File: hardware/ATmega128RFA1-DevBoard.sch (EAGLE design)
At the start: 50 parts, among them J1 ISP, J2 ARDUINO_UNO_R3, J3 POWER_JACKPTH_LOCK, U1 ATMEGA128RFA1, U2 LM1117, Y1 16MHz, Y2 32.768kHz

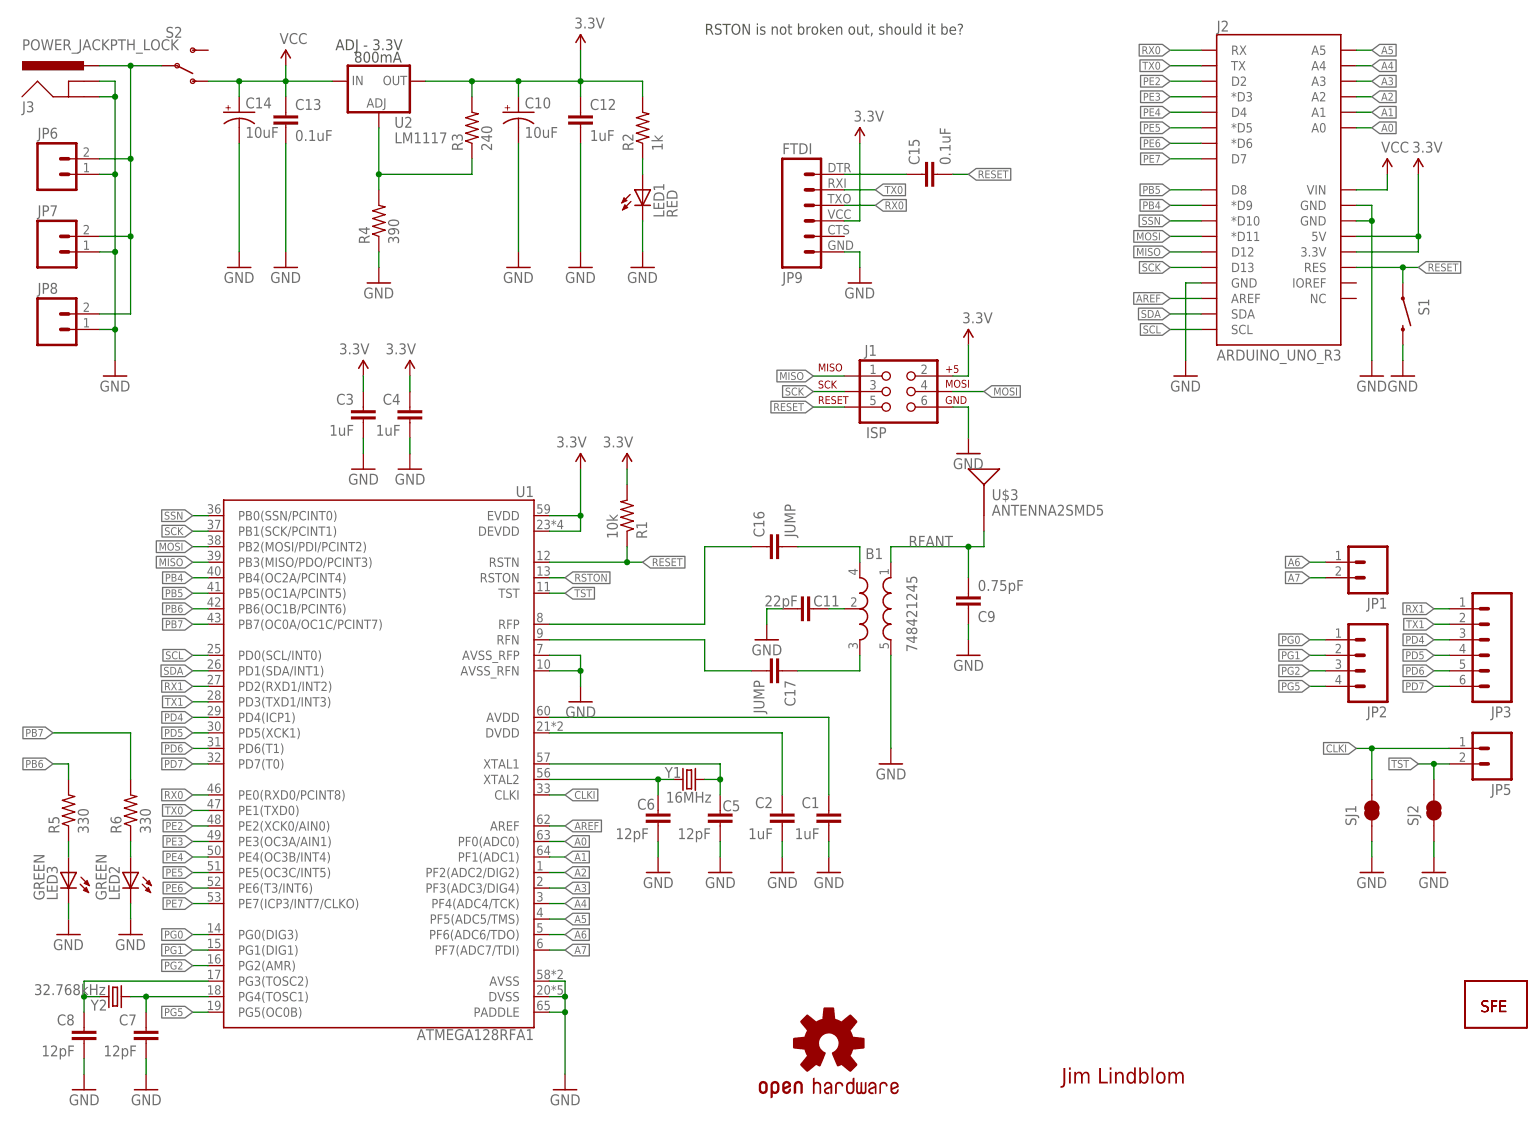
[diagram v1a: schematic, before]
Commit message: More minor silkscreen fixes
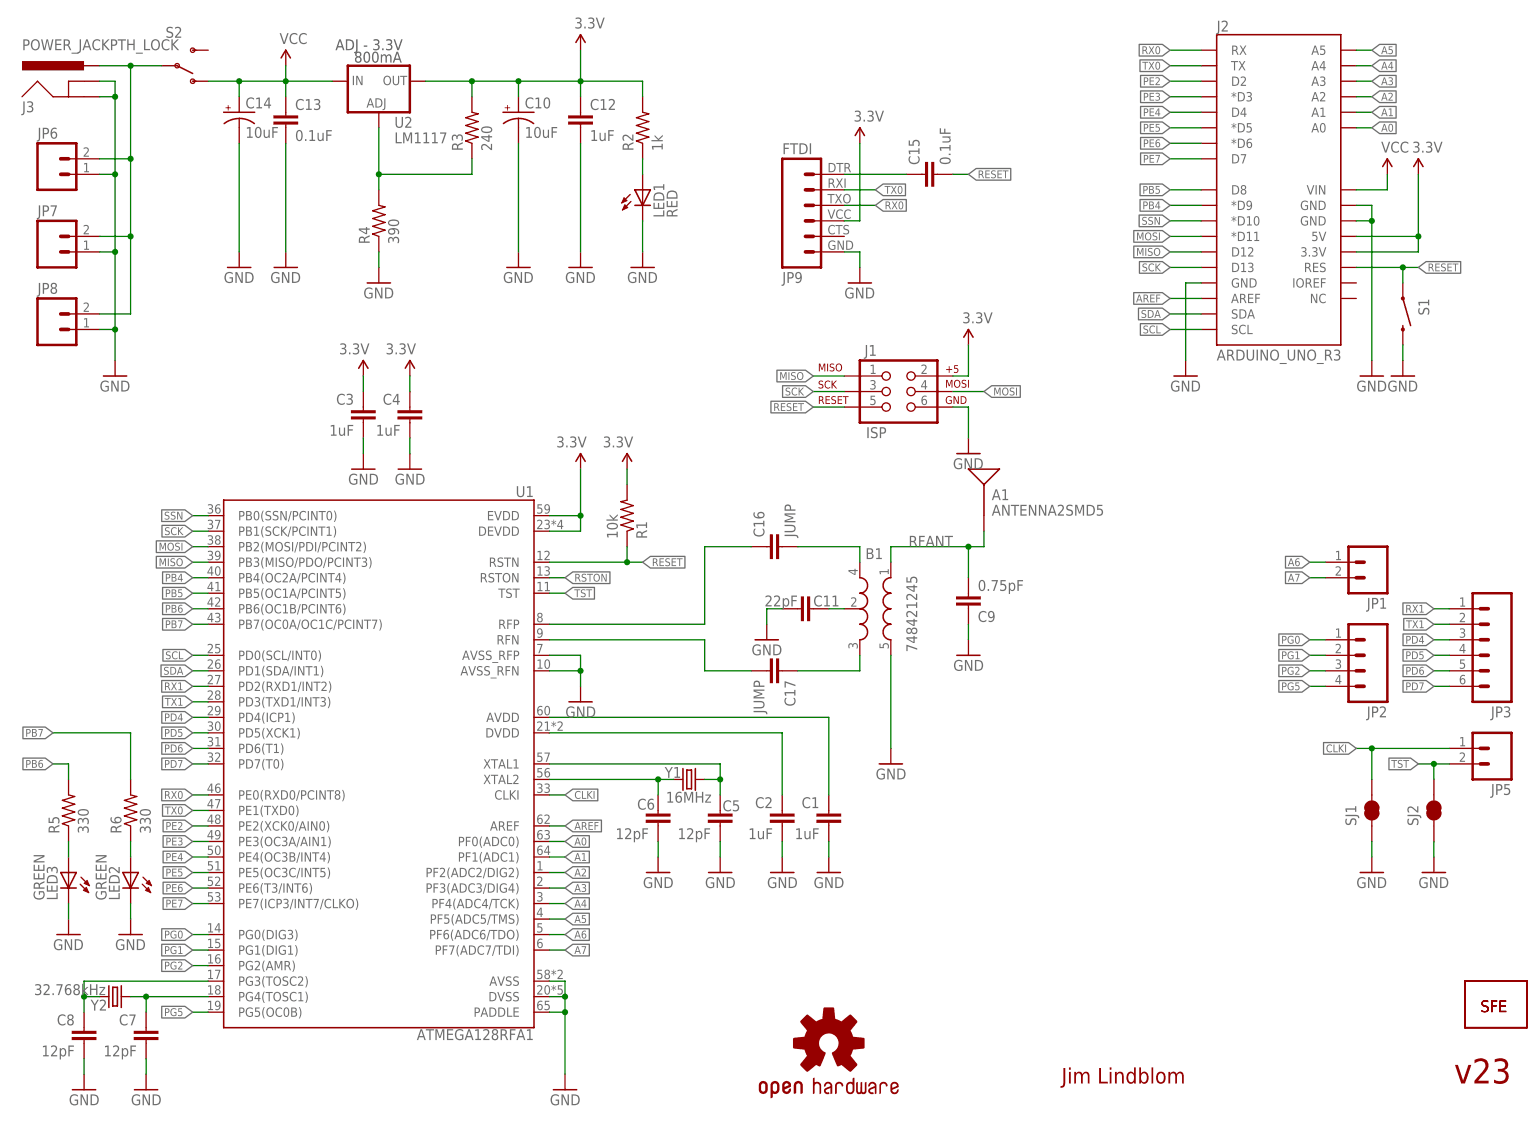
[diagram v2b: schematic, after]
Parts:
- renumbered U$3 to A1
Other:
- note added: "v23"
- note removed: "RSTON is not broken out, should it be?"
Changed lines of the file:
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@@
 <grid distance="0.1" unitdist="inch" unit="inch" style="lines" multiple="1" display="no" altdistance="0.01" altunitdist="inch" altunit="inch"/>
 <layers>
-<layer number="1" name="Top" color="4" fill="1" visible="yes" active="no"/>
-<layer number="2" name="Route2" color="1" fill="3" visible="yes" active="no"/>
-<layer number="3" name="Route3" color="4" fill="3" visible="yes" active="no"/>
-<layer number="4" name="Route4" color="1" fill="4" visible="yes" active="no"/>
-<layer number="5" name="Route5" color="4" fill="4" visible="yes" active="no"/>
-<layer number="6" name="Route6" color="1" fill="8" visible="yes" active="no"/>
-<layer number="7" name="Route7" color="4" fill="8" visible="yes" active="no"/>
-<layer number="8" name="Route8" color="1" fill="2" visible="yes" active="no"/>
-<layer number="9" name="Route9" color="4" fill="2" visible="yes" active="no"/>
-<layer number="10" name="Route10" color="1" fill="7" visible="yes" active="no"/>
-<layer number="11" name="Route11" color="4" fill="7" visible="yes" active="no"/>
-<layer number="12" name="Route12" color="1" fill="5" visible="yes" active="no"/>
-<layer number="13" name="Route13" color="4" fill="5" visible="yes" active="no"/>
-<layer number="14" name="Route14" color="1" fill="6" visible="yes" active="no"/>
-<layer number="15" name="Route15" color="4" fill="6" visible="yes" active="no"/>
-<layer number="16" name="Bottom" color="1" fill="1" visible="yes" active="no"/>
-<layer number="17" name="Pads" color="2" fill="1" visible="yes" active="no"/>
-<layer number="18" name="Vias" color="2" fill="1" visible="yes" active="no"/>
-<layer number="19" name="Unrouted" color="6" fill="1" visible="yes" active="no"/>
-<layer number="20" name="Dimension" color="15" fill="1" visible="yes" active="no"/>
-<layer number="21" name="tPlace" color="16" fill="1" visible="yes" active="no"/>
-<layer number="22" name="bPlace" color="14" fill="1" visible="yes" active="no"/>
-<layer number="23" name="tOrigins" color="15" fill="1" visible="yes" active="no"/>
-<layer number="24" name="bOrigins" color="15" fill="1" visible="yes" active="no"/>
-<layer number="25" name="tNames" color="7" fill="1" visible="yes" active="no"/>
-<layer number="26" name="bNames" color="7" fill="1" visible="yes" active="no"/>
-<layer number="27" name="tValues" color="7" fill="1" visible="yes" active="no"/>
-<layer number="28" name="bValues" color="7" fill="1" visible="yes" active="no"/>
+<layer number="1" name="Top" color="4" fill="1" visible="no" active="no"/>
+<layer number="2" name="Route2" color="1" fill="3" visible="no" active="no"/>
+<layer number="3" name="Route3" color="4" fill="3" visible="no" active="no"/>
+<layer number="4" name="Route4" color="1" fill="4" visible="no" active="no"/>
+<layer number="5" name="Route5" color="4" fill="4" visible="no" active="no"/>
+<layer number="6" name="Route6" color="1" fill="8" visible="no" active="no"/>
+<layer number="7" name="Route7" color="4" fill="8" visible="no" active="no"/>
+<layer number="8" name="Route8" color="1" fill="2" visible="no" active="no"/>
+<layer number="9" name="Route9" color="4" fill="2" visible="no" active="no"/>
+<layer number="10" name="Route10" color="1" fill="7" visible="no" active="no"/>
+<layer number="11" name="Route11" color="4" fill="7" visible="no" active="no"/>
+<layer number="12" name="Route12" color="1" fill="5" visible="no" active="no"/>
+<layer number="13" name="Route13" color="4" fill="5" visible="no" active="no"/>
+<layer number="14" name="Route14" color="1" fill="6" visible="no" active="no"/>
+<layer number="15" name="Route15" color="4" fill="6" visible="no" active="no"/>
+<layer number="16" name="Bottom" color="1" fill="1" visible="no" active="no"/>
+<layer number="17" name="Pads" color="2" fill="1" visible="no" active="no"/>
+<layer number="18" name="Vias" color="2" fill="1" visible="no" active="no"/>
+<layer number="19" name="Unrouted" color="6" fill="1" visible="no" active="no"/>
+<layer number="20" name="Dimension" color="15" fill="1" visible="no" active="no"/>
+<layer number="21" name="tPlace" color="16" fill="1" visible="no" active="no"/>
+<layer number="22" name="bPlace" color="14" fill="1" visible="no" active="no"/>
+<layer number="23" name="tOrigins" color="15" fill="1" visible="no" active="no"/>
+<layer number="24" name="bOrigins" color="15" fill="1" visible="no" active="no"/>
+<layer number="25" name="tNames" color="7" fill="1" visible="no" active="no"/>
+<layer number="26" name="bNames" color="7" fill="1" visible="no" active="no"/>
+<layer number="27" name="tValues" color="7" fill="1" visible="no" active="no"/>
+<layer number="28" name="bValues" color="7" fill="1" visible="no" active="no"/>
 <layer number="29" name="tStop" color="7" fill="3" visible="no" active="no"/>
 <layer number="30" name="bStop" color="7" fill="6" visible="no" active="no"/>
@@
 <layer number="35" name="tGlue" color="7" fill="4" visible="no" active="no"/>
 <layer number="36" name="bGlue" color="7" fill="5" visible="no" active="no"/>
-<layer number="37" name="tTest" color="7" fill="1" visible="yes" active="no"/>
-<layer number="38" name="bTest" color="7" fill="1" visible="yes" active="no"/>
+<layer number="37" name="tTest" color="7" fill="1" visible="no" active="no"/>
+<layer number="38" name="bTest" color="7" fill="1" visible="no" active="no"/>
 <layer number="39" name="tKeepout" color="4" fill="11" visible="no" active="no"/>
 <layer number="40" name="bKeepout" color="1" fill="11" visible="no" active="no"/>
@@
 <layer number="44" name="Drills" color="7" fill="1" visible="no" active="no"/>
 <layer number="45" name="Holes" color="7" fill="1" visible="no" active="no"/>
-<layer number="46" name="Milling" color="3" fill="1" visible="yes" active="no"/>
-<layer number="47" name="Measures" color="7" fill="1" visible="yes" active="no"/>
-<layer number="48" name="Document" color="7" fill="1" visible="yes" active="no"/>
-<layer number="49" name="Reference" color="7" fill="1" visible="yes" active="no"/>
-<layer number="50" name="dxf" color="7" fill="1" visible="yes" active="no"/>
-<layer number="51" name="tDocu" color="6" fill="1" visible="yes" active="no"/>
-<layer number="52" name="bDocu" color="7" fill="1" visible="yes" active="no"/>
-<layer number="53" name="tGND_GNDA" color="7" fill="9" visible="yes" active="no"/>
-<layer number="54" name="bGND_GNDA" color="1" fill="9" visible="yes" active="no"/>
-<layer number="56" name="wert" color="7" fill="1" visible="yes" active="no"/>
+<layer number="46" name="Milling" color="3" fill="1" visible="no" active="no"/>
+<layer number="47" name="Measures" color="7" fill="1" visible="no" active="no"/>
+<layer number="48" name="Document" color="7" fill="1" visible="no" active="no"/>
+<layer number="49" name="Reference" color="7" fill="1" visible="no" active="no"/>
+<layer number="50" name="dxf" color="7" fill="1" visible="no" active="no"/>
+<layer number="51" name="tDocu" color="6" fill="1" visible="no" active="no"/>
+<layer number="52" name="bDocu" color="7" fill="1" visible="no" active="no"/>
+<layer number="53" name="tGND_GNDA" color="7" fill="9" visible="no" active="no"/>
+<layer number="54" name="bGND_GNDA" color="1" fill="9" visible="no" active="no"/>
+<layer number="56" name="wert" color="7" fill="1" visible="no" active="no"/>
 <layer number="91" name="Nets" color="2" fill="1" visible="yes" active="yes"/>
 <layer number="92" name="Busses" color="1" fill="1" visible="yes" active="yes"/>
@@
 <part name="GND31" library="SparkFun" deviceset="GND" device=""/>
 <part name="JP4" library="SparkFun-Aesthetics" deviceset="LOGO-SFE" device="NEW"/>
-<part name="U$3" library="SparkFun-RF" deviceset="ANTENNA2" device="SMD5"/>
+<part name="A1" library="SparkFun-RF" deviceset="ANTENNA2" device="SMD5"/>
 </parts>
 <sheets>
@@
 <text x="56.896" y="173.228" size="1.778" layer="97">800mA</text>
 <text x="53.848" y="175.26" size="1.778" layer="97">ADJ - 3.3V</text>
-<text x="114.3" y="177.8" size="1.778" layer="97">RSTON is not broken out, should it be?</text>
+<text x="236.982" y="6.096" size="4.064" layer="94">v23</text>
 </plain>
 <instances>
@@
 <instance part="GND31" gate="1" x="20.32" y="30.48"/>
 <instance part="JP4" gate="G$1" x="241.3" y="17.78"/>
-<instance part="U$3" gate="G$1" x="160.02" y="101.6"/>
+<instance part="A1" gate="G$1" x="160.02" y="101.6"/>
 </instances>
 <busses>
@@
 <wire x1="160.02" y1="93.98" x2="157.48" y2="93.98" width="0.1524" layer="91"/>
 <wire x1="160.02" y1="93.98" x2="160.02" y2="96.52" width="0.1524" layer="91"/>
-<pinref part="U$3" gate="G$1" pin="SIGNAL"/>
-</segment>
-</net>
+<pinref part="A1" gate="G$1" pin="SIGNAL"/>
+</segment>
+</net>
